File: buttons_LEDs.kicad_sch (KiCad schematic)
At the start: 48 parts, among them J12 BTN_KNOB, J13 BTN_KNOB, J14 KNOB_AND_WS, SW4 BTN1, SW5 BTN0, SW6 BTN2, U3 SN74LVC1G14DBV

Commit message: more stuff added to sch
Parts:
- added R38: 10k 1%, Resistor_SMD:R_0603_1608Metric_Pad0.98x0.95mm_HandSolder, symbol Device:R_Small
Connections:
- net +3V3: now also R38.1
- net at J14.1 (Pin_1), U3.2: now also R38.2
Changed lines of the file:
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@@
 	)
 	(junction
+		(at 46.99 39.37)
+		(diameter 0)
+		(color 0 0 0 0)
+	)
+	(junction
 		(at 144.78 22.86)
 		(diameter 0)
@@
 	(wire
 		(pts
+			(xy 46.99 30.48) (xy 46.99 39.37)
+		)
+		(stroke
+			(width 0)
+			(type default)
+		)
+	)
+	(wire
+		(pts
 			(xy 226.06 46.99) (xy 226.06 48.26)
 		)
@@
 	(wire
 		(pts
+			(xy 46.99 24.13) (xy 46.99 25.4)
+		)
+		(stroke
+			(width 0)
+			(type default)
+		)
+	)
+	(wire
+		(pts
 			(xy 158.75 22.86) (xy 165.1 22.86)
 		)
@@
 	)
 	(symbol
+		(lib_id "power:+3.3V")
+		(at 46.99 24.13 0)
+		(unit 1)
+		(exclude_from_sim no)
+		(in_bom yes)
+		(on_board yes)
+		(dnp no)
+		(property "Reference" "#PWR0212"
+			(at 46.99 27.94 0)
+			(effects
+				(font
+					(size 1.27 1.27)
+				)
+				(hide yes)
+			)
+		)
+		(property "Value" "+3V3"
+			(at 46.99 20.32 0)
+			(effects
+				(font
+					(size 1.27 1.27)
+				)
+			)
+		)
+		(property "Footprint" ""
+			(at 46.99 24.13 0)
+			(effects
+				(font
+					(size 1.27 1.27)
+				)
+				(hide yes)
+			)
+		)
+		(property "Datasheet" ""
+			(at 46.99 24.13 0)
+			(effects
+				(font
+					(size 1.27 1.27)
+				)
+				(hide yes)
+			)
+		)
+		(property "Description" ""
+			(at 46.99 24.13 0)
+			(effects
+				(font
+					(size 1.27 1.27)
+				)
+				(hide yes)
+			)
+		)
+		(pin "1"
+		)
+		(instances
+			(project "beam_kit_1"
+				(path "/3a707576-1044-44db-8cf8-deb84fe605c8/068b0987-b1c9-47c8-b32e-252cfc200213"
+					(reference "#PWR0212")
+					(unit 1)
+				)
+			)
+		)
+	)
+	(symbol
 		(lib_id "Device:C_Small")
 		(at 118.11 26.67 0)
@@
 					(unit 1)
 				)
+			)
+		)
+	)
+	(symbol
+		(lib_id "Device:R_Small")
+		(at 46.99 27.94 0)
+		(unit 1)
+		(exclude_from_sim no)
+		(in_bom yes)
+		(on_board yes)
+		(dnp no)
+		(property "Reference" "R38"
+			(at 48.26 26.67 0)
+			(effects
+				(font
+					(size 1.27 1.27)
+				)
+				(justify left)
+			)
+		)
+		(property "Value" "10k 1%"
+			(at 48.26 29.21 0)
+			(effects
+				(font
+					(size 1.27 1.27)
+				)
+				(justify left)
+			)
+		)
+		(property "Footprint" "Resistor_SMD:R_0603_1608Metric_Pad0.98x0.95mm_HandSolder"
+			(at 46.99 27.94 0)
+			(effects
+				(font
+					(size 1.27 1.27)
+				)
+				(hide yes)
+			)
+		)
+		(property "Datasheet" "~"
+			(at 46.99 27.94 0)
+			(effects
+				(font
+					(size 1.27 1.27)
+				)
+				(hide yes)
+			)
+		)
+		(property "Description" ""
+			(at 46.99 27.94 0)
+			(effects
+				(font
+					(size 1.27 1.27)
+				)
+				(hide yes)
+			)
+		)
+		(pin "1"
+		)
+		(pin "2"
+		)
+		(instances
+			(project "beam_kit_1"
+				(path "/3a707576-1044-44db-8cf8-deb84fe605c8/068b0987-b1c9-47c8-b32e-252cfc200213"
+					(reference "R38")
+					(unit 1)
+				)

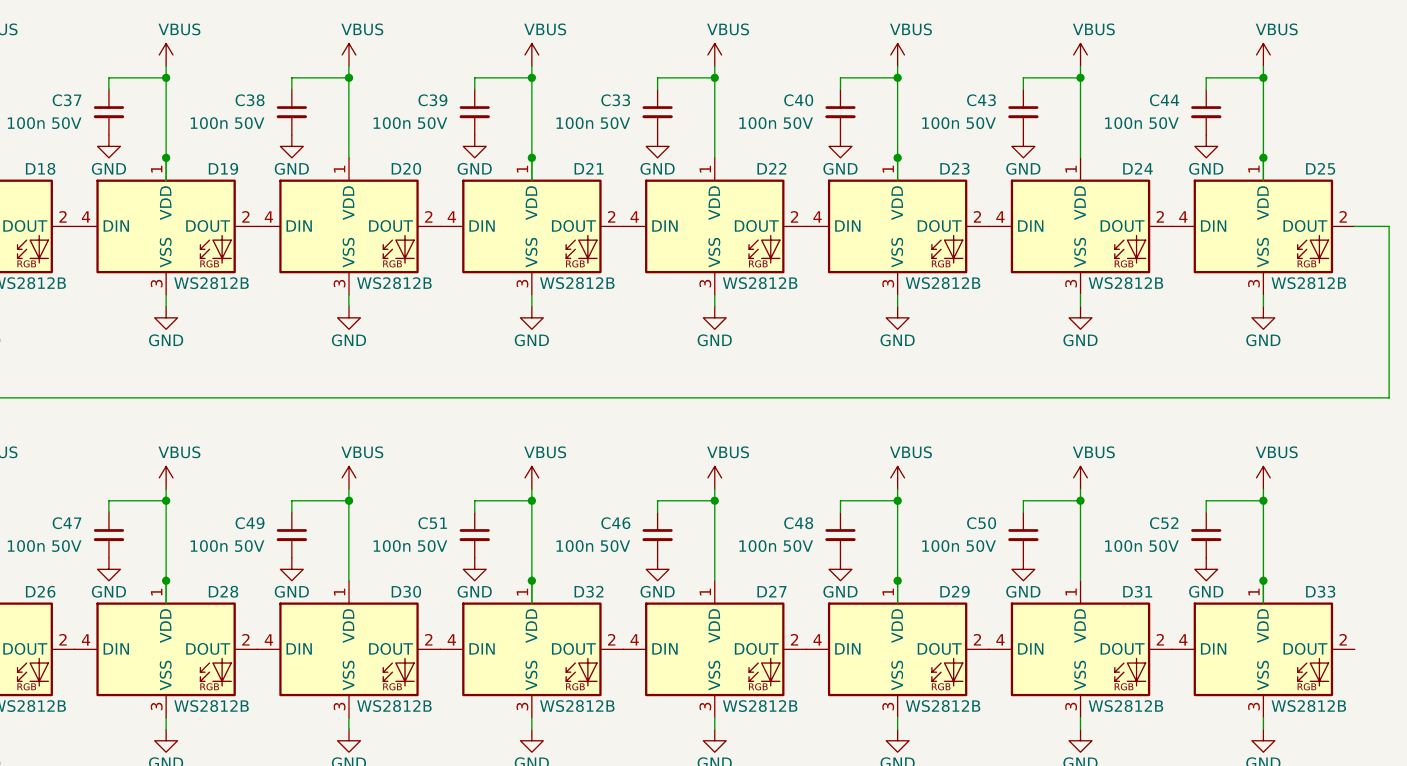
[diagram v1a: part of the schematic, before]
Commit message: kju fix and PCB size increase
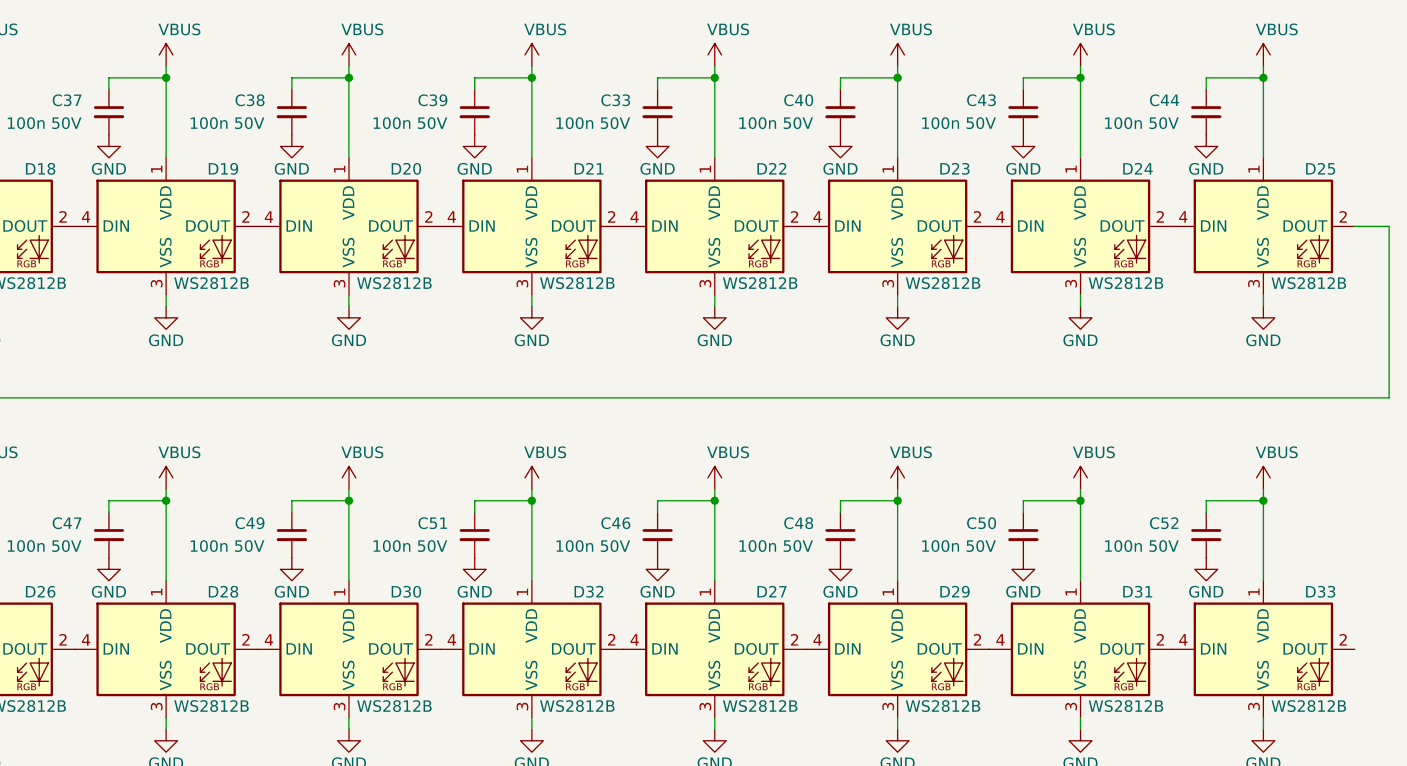
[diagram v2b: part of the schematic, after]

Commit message: codes and fixes
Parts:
- C33, C36, C37, C38, C39, C40, C43, C44, C45, C46, C47, C48, C49, C50, C51, C52: value 100n 50V -> 100n 16V; jlc C307331 -> C1525
- C41, C42: footprint Capacitor_SMD:C_0603_1608Metric -> Capacitor_SMD:C_0603_1608Metric_Pad1.08x0.95mm_HandSolder; jlc (none) -> C14663
- D15, D16, D17: jlc (none) -> C2286
- J12, J13: jlc (none) -> C49257
- J14: jlc (none) -> C492401
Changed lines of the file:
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@@
 			)
 		)
-		(property "Value" "100n 50V"
+		(property "Value" "100n 16V"
 			(at 187.96 27.94 0)
 			(effects
@@
 			)
 		)
-		(property "jlc" "C307331"
+		(property "jlc" "C1525"
 			(at 199.39 26.67 0)
 			(effects
@@
 			)
 		)
+		(property "jlc" "C49257"
+			(at 57.15 138.43 0)
+			(effects
+				(font
+					(size 1.27 1.27)
+				)
+				(hide yes)
+			)
+		)
 		(pin "1"
 		)
@@
 			)
 		)
-		(property "Value" "100n 50V"
+		(property "Value" "100n 16V"
 			(at 147.32 27.94 0)
 			(effects
@@
 			)
 		)
-		(property "jlc" "C307331"
+		(property "jlc" "C1525"
 			(at 158.75 26.67 0)
 			(effects
@@
 			)
 		)
+		(property "jlc" "C2286"
+			(at 57.15 163.83 0)
+			(effects
+				(font
+					(size 1.27 1.27)
+				)
+				(hide yes)
+			)
+		)
 		(pin "1"
 		)
@@
 			)
 		)
-		(property "Value" "100n 50V"
+		(property "Value" "100n 16V"
 			(at 167.64 27.94 0)
 			(effects
@@
 			)
 		)
-		(property "jlc" "C307331"
+		(property "jlc" "C1525"
 			(at 179.07 26.67 0)
 			(effects
@@
 			)
 		)
-		(property "Value" "100n 50V"
+		(property "Value" "100n 16V"
 			(at 167.64 74.93 0)
 			(effects
@@
 			)
 		)
-		(property "jlc" "C307331"
+		(property "jlc" "C1525"
 			(at 179.07 73.66 0)
 			(effects
@@
 			)
 		)
-		(property "Value" "100n 50V"
+		(property "Value" "100n 16V"
 			(at 248.92 27.94 0)
 			(effects
@@
 			)
 		)
-		(property "jlc" "C307331"
+		(property "jlc" "C1525"
 			(at 260.35 26.67 0)
 			(effects
@@
 			)
 		)
-		(property "Footprint" "Capacitor_SMD:C_0603_1608Metric"
+		(property "Footprint" "Capacitor_SMD:C_0603_1608Metric_Pad1.08x0.95mm_HandSolder"
 			(at 66.04 72.39 0)
 			(effects
@@
 			)
 		)
+		(property "jlc" "C14663"
+			(at 66.04 72.39 0)
+			(effects
+				(font
+					(size 1.27 1.27)
+				)
+				(hide yes)
+			)
+		)
 		(pin "1"
 		)
@@
 			)
 		)
-		(property "Value" "100n 50V"
+		(property "Value" "100n 16V"
 			(at 147.32 74.93 0)
 			(effects
@@
 			)
 		)
-		(property "jlc" "C307331"
+		(property "jlc" "C1525"
 			(at 158.75 73.66 0)
 			(effects
@@
 			)
 		)
-		(property "Value" "100n 50V"
+		(property "Value" "100n 16V"
 			(at 248.92 74.93 0)
 			(effects
@@
 			)
 		)
-		(property "jlc" "C307331"
+		(property "jlc" "C1525"
 			(at 260.35 73.66 0)
 			(effects
@@
 			)
 		)
+		(property "jlc" "C492401"
+			(at 35.56 53.34 0)
+			(effects
+				(font
+					(size 1.27 1.27)
+				)
+				(hide yes)
+			)
+		)
 		(pin "2"
 		)
@@
 			)
 		)
-		(property "Value" "100n 50V"
+		(property "Value" "100n 16V"
 			(at 107.696 75.692 0)
 			(effects
@@
 			)
 		)
-		(property "jlc" "C307331"
+		(property "jlc" "C1525"
 			(at 118.11 73.66 0)
 			(effects
@@
 			)
 		)
-		(property "Value" "100n 50V"
+		(property "Value" "100n 16V"
 			(at 228.6 27.94 0)
 			(effects
@@
 			)
 		)
-		(property "jlc" "C307331"
+		(property "jlc" "C1525"
 			(at 240.03 26.67 0)
 			(effects
@@
 			)
 		)
-		(property "Value" "100n 50V"
+		(property "Value" "100n 16V"
 			(at 106.68 27.94 0)
 			(effects
@@
 			)
 		)
-		(property "jlc" "C307331"
+		(property "jlc" "C1525"
 			(at 118.11 26.67 0)
 			(effects
@@
 			)
 		)
-		(property "Footprint" "Capacitor_SMD:C_0603_1608Metric"
+		(property "Footprint" "Capacitor_SMD:C_0603_1608Metric_Pad1.08x0.95mm_HandSolder"
 			(at 63.5 30.48 0)
 			(effects
@@
 			)
 		)
+		(property "jlc" "C14663"
+			(at 63.5 30.48 0)
+			(effects
+				(font
+					(size 1.27 1.27)
+				)
+				(hide yes)
+			)
+		)
 		(pin "1"
 		)
@@
 			)
 		)
+		(property "jlc" "C2286"
+			(at 45.72 163.83 0)
+			(effects
+				(font
+					(size 1.27 1.27)
+				)
+				(hide yes)
+			)
+		)
 		(pin "1"
 		)
@@
 			)
 		)
-		(property "Value" "100n 50V"
+		(property "Value" "100n 16V"
 			(at 208.28 74.93 0)
 			(effects
@@
 			)
 		)
-		(property "jlc" "C307331"
+		(property "jlc" "C1525"
 			(at 219.71 73.66 0)
 			(effects
@@
 			)
 		)
+		(property "jlc" "C49257"
+			(at 106.68 138.43 0)
+			(effects
+				(font
+					(size 1.27 1.27)
+				)
+				(hide yes)
+			)
+		)
 		(pin "1"
 		)
@@
 			)
 		)
+		(property "jlc" "C2286"
+			(at 68.58 163.83 0)
+			(effects
+				(font
+					(size 1.27 1.27)
+				)
+				(hide yes)
+			)
+		)
 		(pin "1"
 		)
@@
 			)
 		)
-		(property "Value" "100n 50V"
+		(property "Value" "100n 16V"
 			(at 127 27.94 0)
 			(effects
@@
 			)
 		)
-		(property "jlc" "C307331"
+		(property "jlc" "C1525"
 			(at 138.43 26.67 0)
 			(effects
@@
 			)
 		)
-		(property "Value" "100n 50V"
+		(property "Value" "100n 16V"
 			(at 228.6 74.93 0)
 			(effects
@@
 			)
 		)
-		(property "jlc" "C307331"
+		(property "jlc" "C1525"
 			(at 240.03 73.66 0)
 			(effects
@@
 			)
 		)
-		(property "Value" "100n 50V"
+		(property "Value" "100n 16V"
 			(at 208.28 27.94 0)
 			(effects
@@
 			)
 		)
-		(property "jlc" "C307331"
+		(property "jlc" "C1525"
 			(at 219.71 26.67 0)
 			(effects
@@
 			)
 		)
-		(property "Value" "100n 50V"
+		(property "Value" "100n 16V"
 			(at 187.96 74.93 0)
 			(effects
@@
 			)
 		)
-		(property "jlc" "C307331"
+		(property "jlc" "C1525"
 			(at 199.39 73.66 0)
 			(effects
@@
 			)
 		)
-		(property "Value" "100n 50V"
+		(property "Value" "100n 16V"
 			(at 127 74.93 0)
 			(effects
@@
 			)
 		)
-		(property "jlc" "C307331"
+		(property "jlc" "C1525"
 			(at 138.43 73.66 0)
 			(effects

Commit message: jlc codes filled
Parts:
- R14, R15, R20: jlc (none) -> C23186
- R38: jlc (none) -> C25804
- SW4, SW5, SW6: jlc (none) -> C455112
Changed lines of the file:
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@@
 			)
 		)
+		(property "jlc" "C23186"
+			(at 45.72 156.21 0)
+			(effects
+				(font
+					(size 1.27 1.27)
+				)
+				(hide yes)
+			)
+		)
 		(pin "1"
 		)
@@
 			)
 		)
+		(property "jlc" "C23186"
+			(at 57.15 156.21 0)
+			(effects
+				(font
+					(size 1.27 1.27)
+				)
+				(hide yes)
+			)
+		)
 		(pin "1"
 		)
@@
 			)
 		)
+		(property "jlc" "C23186"
+			(at 68.58 156.21 0)
+			(effects
+				(font
+					(size 1.27 1.27)
+				)
+				(hide yes)
+			)
+		)
 		(pin "1"
 		)
@@
 			)
 		)
+		(property "jlc" "C25804"
+			(at 46.99 27.94 0)
+			(effects
+				(font
+					(size 1.27 1.27)
+				)
+				(hide yes)
+			)
+		)
 		(pin "1"
 		)
@@
 			)
 		)
+		(property "jlc" "C455112"
+			(at 106.68 162.56 0)
+			(effects
+				(font
+					(size 1.27 1.27)
+				)
+				(hide yes)
+			)
+		)
 		(pin "1"
 		)
@@
 			)
 		)
+		(property "jlc" "C455112"
+			(at 123.19 162.56 0)
+			(effects
+				(font
+					(size 1.27 1.27)
+				)
+				(hide yes)
+			)
+		)
 		(pin "1"
 		)
@@
 			(at 91.44 162.56 0)
 			(effects
+				(font
+					(size 1.27 1.27)
+				)
+				(hide yes)
+			)
+		)
+		(property "jlc" "C455112"
+			(at 91.44 162.56 0)
+			(effects

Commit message: routing in progress
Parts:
- renumbered D22 to D19, D26 to D20, D27 to D21, D19 to D22, D28 to D24, D29 to D25, D20 to D26, D24 to D27, D30 to D28, D31 to D29, D21 to D30, D25 to D31
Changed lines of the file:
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@@
 		(on_board yes)
 		(dnp no)
-		(property "Reference" "D22"
+		(property "Reference" "D19"
 			(at 212.09 33.02 0)
 			(effects
@@
 			(project "beam_kit_1"
 				(path "/3a707576-1044-44db-8cf8-deb84fe605c8/068b0987-b1c9-47c8-b32e-252cfc200213"
-					(reference "D22")
+					(reference "D19")
 					(unit 1)
 				)
@@
 		(on_board yes)
 		(dnp no)
-		(property "Reference" "D20"
+		(property "Reference" "D26"
 			(at 171.45 33.02 0)
 			(effects
@@
 			(project "beam_kit_1"
 				(path "/3a707576-1044-44db-8cf8-deb84fe605c8/068b0987-b1c9-47c8-b32e-252cfc200213"
-					(reference "D20")
+					(reference "D26")
 					(unit 1)
 				)
@@
 		(on_board yes)
 		(dnp no)
-		(property "Reference" "D24"
+		(property "Reference" "D27"
 			(at 252.73 33.02 0)
 			(effects
@@
 			(project "beam_kit_1"
 				(path "/3a707576-1044-44db-8cf8-deb84fe605c8/068b0987-b1c9-47c8-b32e-252cfc200213"
-					(reference "D24")
+					(reference "D27")
 					(unit 1)
 				)
@@
 		(on_board yes)
 		(dnp no)
-		(property "Reference" "D28"
+		(property "Reference" "D24"
 			(at 151.13 80.01 0)
 			(effects
@@
 			(project "beam_kit_1"
 				(path "/3a707576-1044-44db-8cf8-deb84fe605c8/068b0987-b1c9-47c8-b32e-252cfc200213"
-					(reference "D28")
+					(reference "D24")
 					(unit 1)
 				)
@@
 		(on_board yes)
 		(dnp no)
-		(property "Reference" "D27"
+		(property "Reference" "D21"
 			(at 212.09 80.01 0)
 			(effects
@@
 			(project "beam_kit_1"
 				(path "/3a707576-1044-44db-8cf8-deb84fe605c8/068b0987-b1c9-47c8-b32e-252cfc200213"
-					(reference "D27")
+					(reference "D21")
 					(unit 1)
 				)
@@
 		(on_board yes)
 		(dnp no)
-		(property "Reference" "D21"
+		(property "Reference" "D30"
 			(at 191.77 33.02 0)
 			(effects
@@
 			(project "beam_kit_1"
 				(path "/3a707576-1044-44db-8cf8-deb84fe605c8/068b0987-b1c9-47c8-b32e-252cfc200213"
-					(reference "D21")
+					(reference "D30")
 					(unit 1)
 				)
@@
 		(on_board yes)
 		(dnp no)
-		(property "Reference" "D30"
+		(property "Reference" "D28"
 			(at 171.45 80.01 0)
 			(effects
@@
 			(project "beam_kit_1"
 				(path "/3a707576-1044-44db-8cf8-deb84fe605c8/068b0987-b1c9-47c8-b32e-252cfc200213"
-					(reference "D30")
+					(reference "D28")
 					(unit 1)
 				)
@@
 		(on_board yes)
 		(dnp no)
-		(property "Reference" "D26"
+		(property "Reference" "D20"
 			(at 130.81 80.01 0)
 			(effects
@@
 			(project "beam_kit_1"
 				(path "/3a707576-1044-44db-8cf8-deb84fe605c8/068b0987-b1c9-47c8-b32e-252cfc200213"
-					(reference "D26")
+					(reference "D20")
 					(unit 1)
 				)
@@
 		(on_board yes)
 		(dnp no)
-		(property "Reference" "D31"
+		(property "Reference" "D29"
 			(at 252.73 80.01 0)
 			(effects
@@
 			(project "beam_kit_1"
 				(path "/3a707576-1044-44db-8cf8-deb84fe605c8/068b0987-b1c9-47c8-b32e-252cfc200213"
-					(reference "D31")
+					(reference "D29")
 					(unit 1)
 				)
@@
 		(on_board yes)
 		(dnp no)
-		(property "Reference" "D25"
+		(property "Reference" "D31"
 			(at 273.05 33.02 0)
 			(effects
@@
 			(project "beam_kit_1"
 				(path "/3a707576-1044-44db-8cf8-deb84fe605c8/068b0987-b1c9-47c8-b32e-252cfc200213"
-					(reference "D25")
+					(reference "D31")
 					(unit 1)
 				)
@@
 		(on_board yes)
 		(dnp no)
-		(property "Reference" "D29"
+		(property "Reference" "D25"
 			(at 232.41 80.01 0)
 			(effects
@@
 			(project "beam_kit_1"
 				(path "/3a707576-1044-44db-8cf8-deb84fe605c8/068b0987-b1c9-47c8-b32e-252cfc200213"
-					(reference "D29")
+					(reference "D25")
 					(unit 1)
 				)
@@
 		(on_board yes)
 		(dnp no)
-		(property "Reference" "D19"
+		(property "Reference" "D22"
 			(at 151.13 33.02 0)
 			(effects
@@
 			(project "beam_kit_1"
 				(path "/3a707576-1044-44db-8cf8-deb84fe605c8/068b0987-b1c9-47c8-b32e-252cfc200213"
-					(reference "D19")
+					(reference "D22")
 					(unit 1)
 				)

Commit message: layout done
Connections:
- net +3V3 renamed +3.3V
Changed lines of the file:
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@@
+	)
+	(symbol
+		(lib_id "power:+3.3V")
+		(at 46.99 24.13 0)
+		(unit 1)
+		(exclude_from_sim no)
+		(in_bom yes)
+		(on_board yes)
+		(dnp no)
+		(property "Reference" "#PWR0133"
+			(at 46.99 27.94 0)
+			(effects
+				(font
+					(size 1.27 1.27)
+				)
+				(hide yes)
+			)
+		)
+		(property "Value" "+3.3V"
+			(at 46.99 20.32 0)
+			(effects
+				(font
+					(size 1.27 1.27)
+				)
+			)
+		)
+		(property "Footprint" ""
+			(at 46.99 24.13 0)
+			(effects
+				(font
+					(size 1.27 1.27)
+				)
+				(hide yes)
+			)
+		)
+		(property "Datasheet" ""
+			(at 46.99 24.13 0)
+			(effects
+				(font
+					(size 1.27 1.27)
+				)
+				(hide yes)
+			)
+		)
+		(property "Description" "Power symbol creates a global label with name \"+3.3V\""
+			(at 46.99 24.13 0)
+			(effects
+				(font
+					(size 1.27 1.27)
+				)
+				(hide yes)
+			)
+		)
+		(pin "1"
+		)
+		(instances
+			(project "beam_kit_1"
+				(path "/3a707576-1044-44db-8cf8-deb84fe605c8/068b0987-b1c9-47c8-b32e-252cfc200213"
+					(reference "#PWR0133")
+					(unit 1)
+				)
+			)
+		)
 	)
 	(symbol
@@
 	)
 	(symbol
+		(lib_id "power:+3.3V")
+		(at 81.28 60.96 0)
+		(unit 1)
+		(exclude_from_sim no)
+		(in_bom yes)
+		(on_board yes)
+		(dnp no)
+		(property "Reference" "#PWR0236"
+			(at 81.28 64.77 0)
+			(effects
+				(font
+					(size 1.27 1.27)
+				)
+				(hide yes)
+			)
+		)
+		(property "Value" "+3.3V"
+			(at 81.28 57.15 0)
+			(effects
+				(font
+					(size 1.27 1.27)
+				)
+			)
+		)
+		(property "Footprint" ""
+			(at 81.28 60.96 0)
+			(effects
+				(font
+					(size 1.27 1.27)
+				)
+				(hide yes)
+			)
+		)
+		(property "Datasheet" ""
+			(at 81.28 60.96 0)
+			(effects
+				(font
+					(size 1.27 1.27)
+				)
+				(hide yes)
+			)
+		)
+		(property "Description" "Power symbol creates a global label with name \"+3.3V\""
+			(at 81.28 60.96 0)
+			(effects
+				(font
+					(size 1.27 1.27)
+				)
+				(hide yes)
+			)
+		)
+		(pin "1"
+		)
+		(instances
+			(project "beam_kit_1"
+				(path "/3a707576-1044-44db-8cf8-deb84fe605c8/068b0987-b1c9-47c8-b32e-252cfc200213"
+					(reference "#PWR0236")
+					(unit 1)
+				)
+			)
+		)
+	)
+	(symbol
 		(lib_id "CANBigPanel-rescue:GND-power")
 		(at 185.42 95.25 0)
@@
 				(path "/3a707576-1044-44db-8cf8-deb84fe605c8/068b0987-b1c9-47c8-b32e-252cfc200213"
 					(reference "#PWR0164")
-					(unit 1)
-				)
-			)
-		)
-	)
-	(symbol
-		(lib_id "power:+3.3V")
-		(at 81.28 60.96 0)
-		(mirror y)
-		(unit 1)
-		(exclude_from_sim no)
-		(in_bom yes)
-		(on_board yes)
-		(dnp no)
-		(property "Reference" "#PWR0133"
-			(at 81.28 64.77 0)
-			(effects
-				(font
-					(size 1.27 1.27)
-				)
-				(hide yes)
-			)
-		)
-		(property "Value" "+3V3"
-			(at 81.28 57.15 0)
-			(effects
-				(font
-					(size 1.27 1.27)
-				)
-			)
-		)
-		(property "Footprint" ""
-			(at 81.28 60.96 0)
-			(effects
-				(font
-					(size 1.27 1.27)
-				)
-				(hide yes)
-			)
-		)
-		(property "Datasheet" ""
-			(at 81.28 60.96 0)
-			(effects
-				(font
-					(size 1.27 1.27)
-				)
-				(hide yes)
-			)
-		)
-		(property "Description" ""
-			(at 81.28 60.96 0)
-			(effects
-				(font
-					(size 1.27 1.27)
-				)
-				(hide yes)
-			)
-		)
-		(pin "1"
-		)
-		(instances
-			(project "beam_kit_1"
-				(path "/3a707576-1044-44db-8cf8-deb84fe605c8/068b0987-b1c9-47c8-b32e-252cfc200213"
-					(reference "#PWR0133")
 					(unit 1)
 				)
@@
 					(unit 1)
 				)
-			)
-		)
-	)
-	(symbol
-		(lib_id "power:+3.3V")
-		(at 46.99 24.13 0)
-		(unit 1)
-		(exclude_from_sim no)
-		(in_bom yes)
-		(on_board yes)
-		(dnp no)
-		(property "Reference" "#PWR0212"
-			(at 46.99 27.94 0)
-			(effects
-				(font
-					(size 1.27 1.27)
-				)
-				(hide yes)
-			)
-		)
-		(property "Value" "+3V3"
-			(at 46.99 20.32 0)
-			(effects
-				(font
-					(size 1.27 1.27)
-				)
-			)
-		)
-		(property "Footprint" ""
-			(at 46.99 24.13 0)
-			(effects
-				(font
-					(size 1.27 1.27)
-				)
-				(hide yes)
-			)
-		)
-		(property "Datasheet" ""
-			(at 46.99 24.13 0)
-			(effects
-				(font
-					(size 1.27 1.27)
-				)
-				(hide yes)
-			)
-		)
-		(property "Description" ""
-			(at 46.99 24.13 0)
-			(effects
-				(font
-					(size 1.27 1.27)
-				)
-				(hide yes)
-			)
-		)
-		(pin "1"
-		)
-		(instances
-			(project "beam_kit_1"
-				(path "/3a707576-1044-44db-8cf8-deb84fe605c8/068b0987-b1c9-47c8-b32e-252cfc200213"
-					(reference "#PWR0212")
-					(unit 1)
-				)
